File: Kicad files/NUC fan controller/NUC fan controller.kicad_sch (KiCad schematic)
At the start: 14 parts, among them J1 M5Atom left, J2 M5Atom right, M1 Fan_4pin, M2 Fan_4pin, M3 Fan_4pin, M4 Fan_4pin, U1 DS18B20U, U2 DS18B20U, U3 DS18B20U

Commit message: Updated schematic
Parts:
- removed M2, M3, M4: Fan_4pin, symbol Motor:Fan_4pin
- removed R4, R5: 4.7k, Resistor_SMD:R_1206_3216Metric_Pad1.42x1.75mm_HandSolder, symbol Highend-plasma-speaker-rescue:R-kicad_project_geiger-cache
- added J?: Fan 3, Connector_PinHeader_2.54mm:PinHeader_1x04_P2.54mm_Vertical, symbol Connector_Generic:Conn_01x04
- added J?: Fan 2, Connector_PinHeader_2.54mm:PinHeader_1x04_P2.54mm_Vertical, symbol Connector_Generic:Conn_01x04
- added J?: Fan 1, Connector_PinHeader_2.54mm:PinHeader_1x04_P2.54mm_Vertical, symbol Connector_Generic:Conn_01x04
- added J?: Fan 4, Connector_PinHeader_2.54mm:PinHeader_1x04_P2.54mm_Vertical, symbol Connector_Generic:Conn_01x04
- added M? (x3): Fan_4pin, symbol Motor:Fan_4pin
- added R? (x2): 4.7k, Resistor_SMD:R_1206_3216Metric_Pad1.42x1.75mm_HandSolder, symbol Highend-plasma-speaker-rescue:R-kicad_project_geiger-cache
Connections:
- net +5V: now also J?.3 (Pin_3), J?.3 (Pin_3), J?.3 (Pin_3), J?.3 (Pin_3), M?.2 (+), M?.2 (+), M?.2 (+), R?.2, R?.2
- net GND: now also J?.4 (Pin_4), J?.4 (Pin_4), J?.4 (Pin_4), J?.4 (Pin_4), M?.1 (-), M?.1 (-), M?.1 (-)
- net at J2.1 (Pin_1), M1.3 (Tacho), R2.1: now also J?.1 (Pin_1)
- net PWM: now reaches J2.2 (Pin_2), M1.4 (PWM)
- net PWM: now also J?.2 (Pin_2), J?.2 (Pin_2), J?.2 (Pin_2), J?.2 (Pin_2), M?.4 (PWM), M?.4 (PWM), M?.4 (PWM)
- net at J1.4 (Pin_4): now also J?.1 (Pin_1), M?.3 (Tacho), R?.1
- net at J1.3 (Pin_3): now also J?.1 (Pin_1), M?.3 (Tacho), R?.1
- net at J1.5 (Pin_5), R3.1: now also J?.1 (Pin_1), M?.3 (Tacho)
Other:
- note added: "Tacho"
- note added: "Tacho 1"
- note added: "Tacho 2"
- note added: "Tacho 3"
- note added: "Tacho 4"
- title: (none) -> Prototype for NUC fan controller
- moved on the sheet: J2, M1, R2, R3

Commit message: Added sensor connectors
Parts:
- added J3: sensor 1 connector, Connector_PinHeader_2.54mm:PinHeader_1x04_P2.54mm_Vertical, symbol Connector_Generic:Conn_01x03
- added J4: sensor 2 connector, Connector_PinHeader_2.54mm:PinHeader_1x04_P2.54mm_Vertical, symbol Connector_Generic:Conn_01x03
- added J5: sensor 3 connector, Connector_PinHeader_2.54mm:PinHeader_1x04_P2.54mm_Vertical, symbol Connector_Generic:Conn_01x03
- gave numbers to parts that had none: 9
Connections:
- net +5V: now also J3.1 (Pin_1), J4.1 (Pin_1), J5.1 (Pin_1)
- net GND: now also J3.2 (Pin_2), J4.2 (Pin_2), J5.2 (Pin_2)
- net at J1.2 (Pin_2), R1.1, U1.1 (DQ)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: now also J3.3 (Pin_3), J4.3 (Pin_3), J5.3 (Pin_3)
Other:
- moved on the sheet: R1, U1

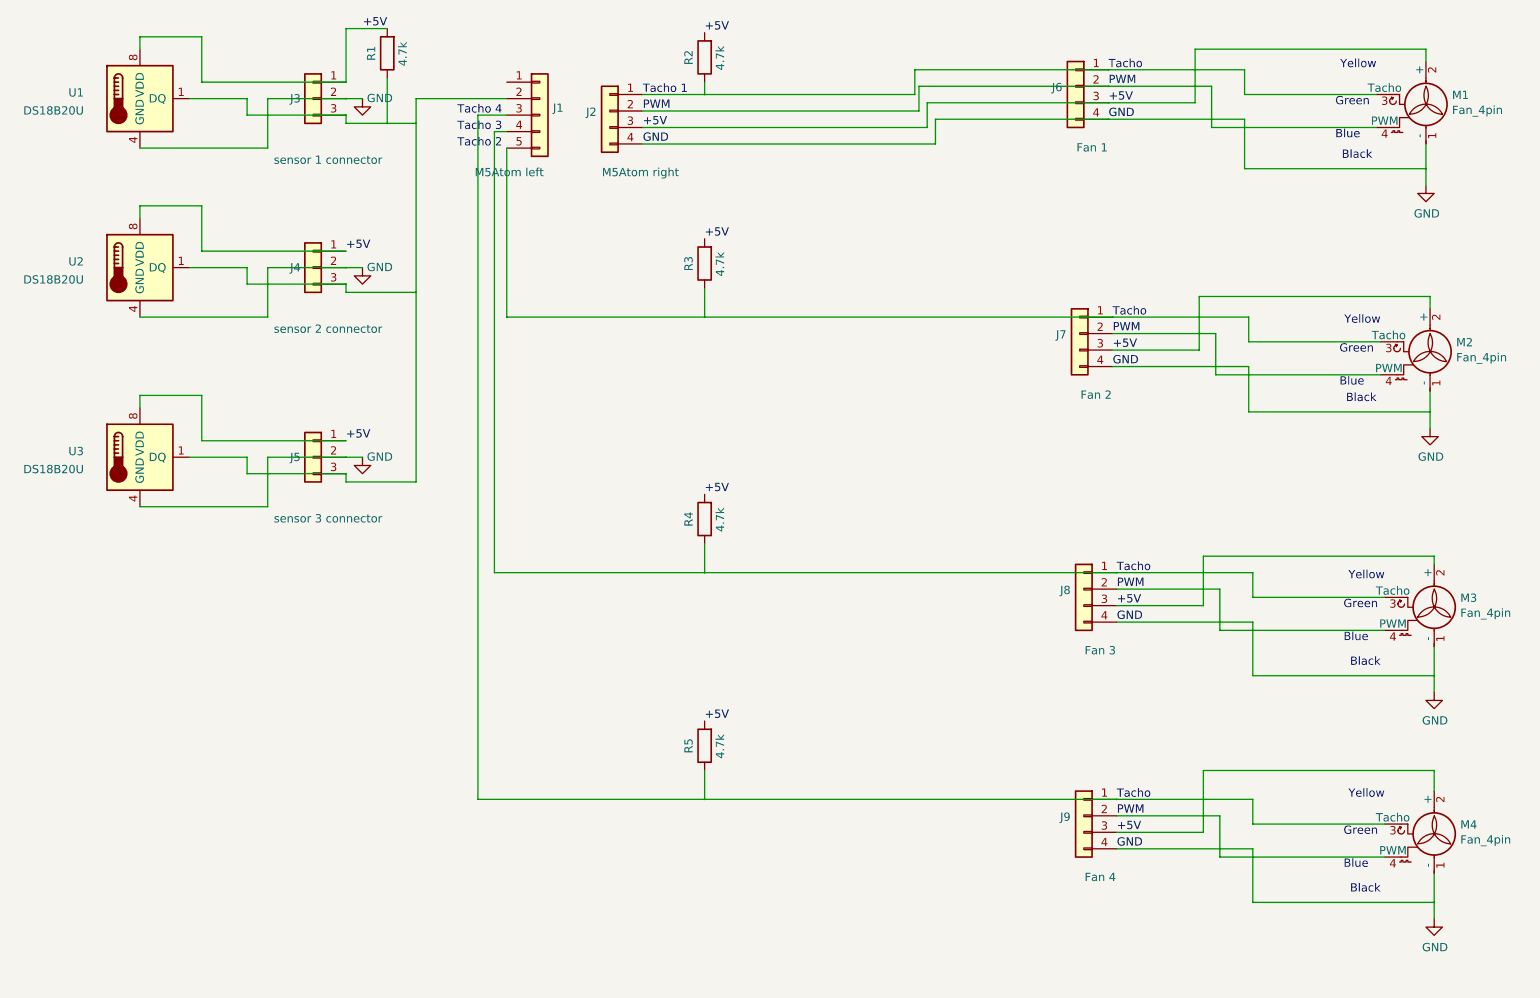
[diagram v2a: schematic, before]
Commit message: Removed extra resistors for schematic and replaced it with software pullups
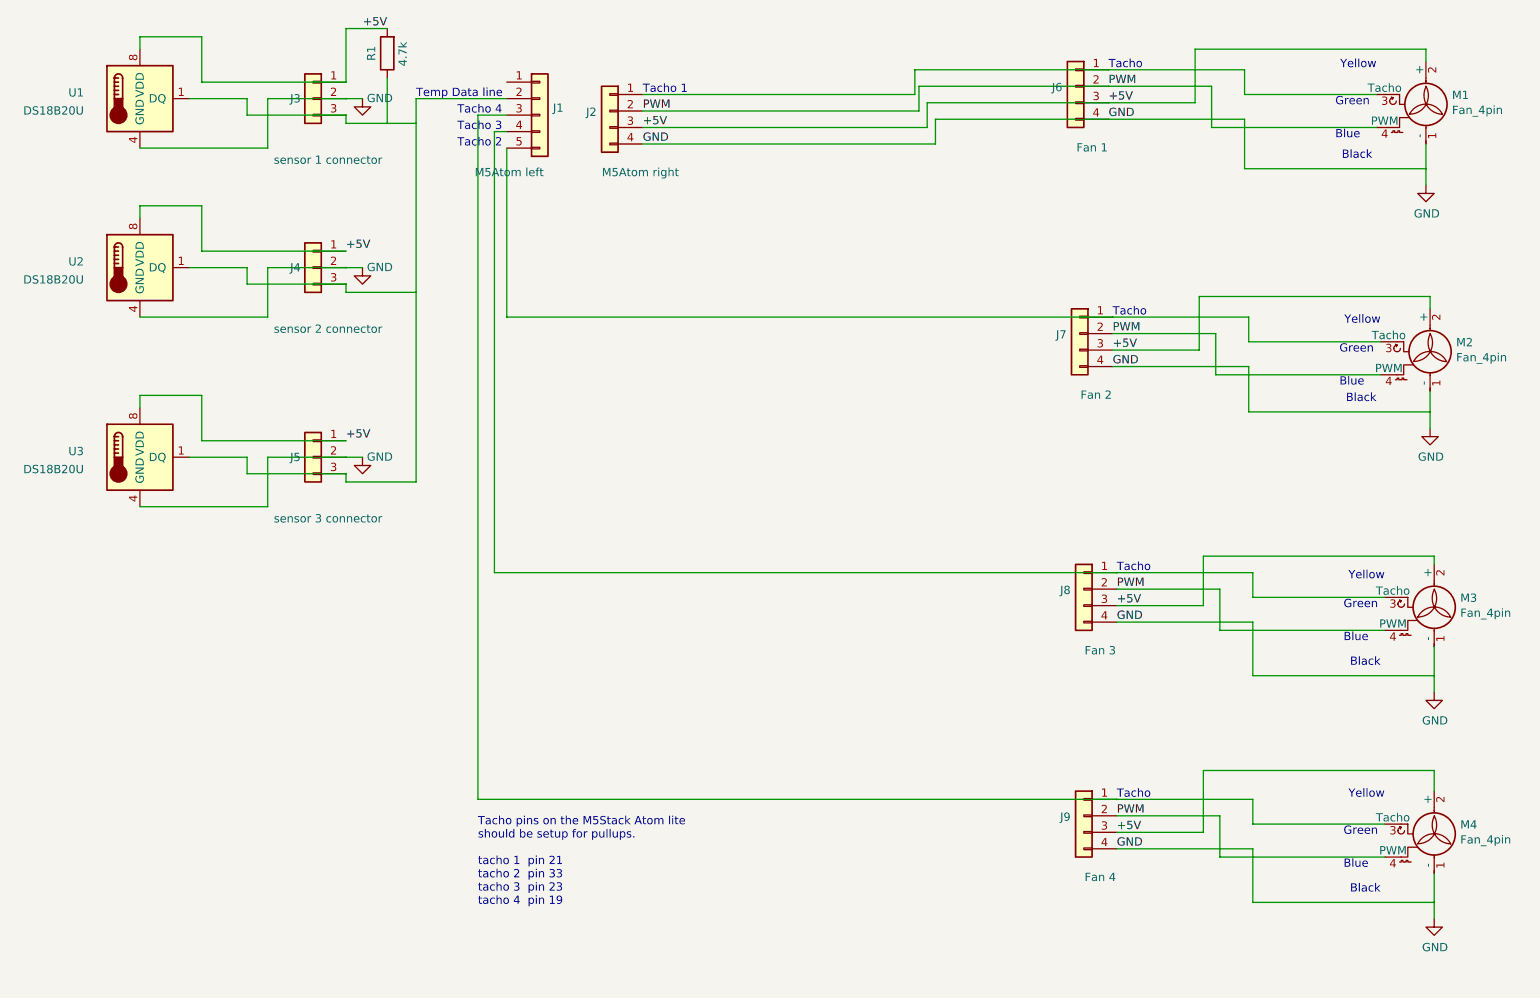
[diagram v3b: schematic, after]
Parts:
- removed R2, R3, R4, R5: 4.7k, Resistor_SMD:R_1206_3216Metric_Pad1.42x1.75mm_HandSolder, symbol Highend-plasma-speaker-rescue:R-kicad_project_geiger-cache
- J3, J4, J5: footprint Connector_PinHeader_2.54mm:PinHeader_1x04_P2.54mm_Vertical -> Connector_PinHeader_2.54mm:PinHeader_1x03_P2.54mm_Vertical
- U1, U2, U3: footprint Package_SO:MSOP-8_3x3mm_P0.65mm -> (none)
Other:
- note added: "Tacho pins on the M5Stack Atom lite should be setup for pullups. tacho 1 pin 21 tacho 2 pin 33 tacho 3 pin 23 tacho 4 pin 19"
- note added: "Temp Data line"

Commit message: Added software pullup on tacho pin. (less resistors needed)
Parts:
- R1: footprint Resistor_SMD:R_1206_3216Metric_Pad1.42x1.75mm_HandSolder -> Resistor_THT:R_Axial_DIN0207_L6.3mm_D2.5mm_P10.16mm_Horizontal
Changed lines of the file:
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@@
       (effects (font (size 1.27 1.27)) (justify left))
     )
-    (property "Footprint" "Resistor_SMD:R_1206_3216Metric_Pad1.42x1.75mm_HandSolder" (id 2) (at 74.803 26.67 90)
+    (property "Footprint" "Resistor_THT:R_Axial_DIN0207_L6.3mm_D2.5mm_P10.16mm_Horizontal" (id 2) (at 74.803 26.67 90)
       (effects (font (size 1.27 1.27)) hide)
     )
@@
     )
     (path "/8f4b9555-69f8-4b08-8acd-ded96ac0fe27"
-      (reference "R1") (unit 1) (value "4.7k") (footprint "Resistor_SMD:R_1206_3216Metric_Pad1.42x1.75mm_HandSolder")
+      (reference "R1") (unit 1) (value "4.7k") (footprint "Resistor_THT:R_Axial_DIN0207_L6.3mm_D2.5mm_P10.16mm_Horizontal")
     )
     (path "/c8915ca2-8fbf-4446-b87e-22dbc3cb724e"

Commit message: Updated schematic
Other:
- note added: "Tacho pins on the M5Stack Atom lite should be setup for pullups. tacho 1 pin 21 tacho 2 pin 33 tacho 3 pin 23 tacho 4 pin 19 temparatute dataline for sensor is on pin 22"
- note removed: "Tacho pins on the M5Stack Atom lite should be setup for pullups. tacho 1 pin 21 tacho 2 pin 33 tacho 3 pin 23 tacho 4 pin 19"
- moved on the sheet: J1
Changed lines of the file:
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@@
     (stroke (width 0) (type solid) (color 0 0 0 0))
   )
-  (wire (pts (xy 77.47 33.655) (xy 77.47 37.465))
-    (stroke (width 0) (type solid) (color 0 0 0 0))
-  )
-  (wire (pts (xy 77.47 33.655) (xy 91.44 33.655))
+  (wire (pts (xy 77.47 33.02) (xy 77.47 37.465))
+    (stroke (width 0) (type solid) (color 0 0 0 0))
+  )
+  (wire (pts (xy 77.47 33.02) (xy 91.44 33.02))
     (stroke (width 0) (type solid) (color 0 0 0 0))
   )
@@
     (stroke (width 0) (type solid) (color 0 0 0 0))
   )
-  (wire (pts (xy 86.995 36.195) (xy 86.995 141.605))
+  (wire (pts (xy 86.995 35.56) (xy 86.995 141.605))
     (stroke (width 0) (type solid) (color 0 0 0 0))
   )
@@
     (stroke (width 0) (type solid) (color 0 0 0 0))
   )
-  (wire (pts (xy 89.535 38.735) (xy 89.535 106.68))
+  (wire (pts (xy 89.535 38.1) (xy 89.535 106.68))
     (stroke (width 0) (type solid) (color 0 0 0 0))
   )
@@
     (stroke (width 0) (type solid) (color 0 0 0 0))
   )
-  (wire (pts (xy 91.44 36.195) (xy 86.995 36.195))
-    (stroke (width 0) (type solid) (color 0 0 0 0))
-  )
-  (wire (pts (xy 91.44 38.735) (xy 89.535 38.735))
-    (stroke (width 0) (type solid) (color 0 0 0 0))
-  )
-  (wire (pts (xy 91.44 41.275) (xy 91.44 67.31))
+  (wire (pts (xy 91.44 35.56) (xy 86.995 35.56))
+    (stroke (width 0) (type solid) (color 0 0 0 0))
+  )
+  (wire (pts (xy 91.44 38.1) (xy 89.535 38.1))
+    (stroke (width 0) (type solid) (color 0 0 0 0))
+  )
+  (wire (pts (xy 91.44 40.64) (xy 91.44 67.31))
     (stroke (width 0) (type solid) (color 0 0 0 0))
   )
@@
     (stroke (width 0) (type solid) (color 0 0 0 0))
   )
-  (text "Temp Data line" (at 77.47 33.655 0)
-    (effects (font (size 1.27 1.27)) (justify left bottom))
-  )
-  (text "Tacho 4" (at 83.82 36.195 0)
-    (effects (font (size 1.27 1.27)) (justify left bottom))
-  )
-  (text "Tacho 3" (at 83.82 38.735 0)
-    (effects (font (size 1.27 1.27)) (justify left bottom))
-  )
-  (text "Tacho 2" (at 83.82 41.275 0)
-    (effects (font (size 1.27 1.27)) (justify left bottom))
-  )
-  (text "Tacho pins on the M5Stack Atom lite \nshould be setup for pullups.\n\ntacho 1  pin 21\ntacho 2  pin 33\ntacho 3  pin 23\ntacho 4  pin 19\n"
+  (text "Temp Data line" (at 77.47 33.02 0)
+    (effects (font (size 1.27 1.27)) (justify left bottom))
+  )
+  (text "Tacho 4" (at 83.82 35.56 0)
+    (effects (font (size 1.27 1.27)) (justify left bottom))
+  )
+  (text "Tacho 3" (at 83.82 38.1 0)
+    (effects (font (size 1.27 1.27)) (justify left bottom))
+  )
+  (text "Tacho 2" (at 83.82 40.64 0)
+    (effects (font (size 1.27 1.27)) (justify left bottom))
+  )
+  (text "Tacho pins on the M5Stack Atom lite \nshould be setup for pullups.\n\ntacho 1  pin 21\ntacho 2  pin 33\ntacho 3  pin 23\ntacho 4  pin 19\n\ntemparatute dataline for sensor is on pin 22\n\n"
     (at 86.995 158.115 0)
     (effects (font (size 1.27 1.27)) (justify left bottom))
@@
     (pin "4")
   )
-  (symbol (lib_id "Connector_Generic:Conn_01x05") (at 96.52 36.195 0) (unit 1)
-    (in_bom yes) (on_board yes)
-    (property "Reference" "J1" (id 0) (at 98.5521 35.0964 0)
-      (effects (font (size 1.27 1.27)) (justify left))
-    )
-    (property "Value" "M5Atom left" (id 1) (at 86.487 45.015 0)
-      (effects (font (size 1.27 1.27)) (justify left))
-    )
-    (property "Footprint" "Connector_PinSocket_2.54mm:PinSocket_1x06_P2.54mm_Vertical" (id 2) (at 96.52 36.195 0)
-      (effects (font (size 1.27 1.27)) hide)
-    )
-    (property "Datasheet" "~" (id 3) (at 96.52 36.195 0)
-      (effects (font (size 1.27 1.27)) hide)
-    )
+  (symbol (lib_id "Connector_Generic:Conn_01x05") (at 96.52 35.56 0) (unit 1)
+    (in_bom yes) (on_board yes)
+    (property "Reference" "J1" (id 0) (at 98.5521 34.4614 0)
+      (effects (font (size 1.27 1.27)) (justify left))
+    )
+    (property "Value" "M5Atom left" (id 1) (at 86.487 44.38 0)
+      (effects (font (size 1.27 1.27)) (justify left))
+    )
+    (property "Footprint" "Connector_PinSocket_2.54mm:PinSocket_1x06_P2.54mm_Vertical" (id 2) (at 96.52 35.56 0)
+      (effects (font (size 1.27 1.27)) hide)
+    )
+    (property "Datasheet" "~" (id 3) (at 96.52 35.56 0)
+      (effects (font (size 1.27 1.27)) hide)
+    )
